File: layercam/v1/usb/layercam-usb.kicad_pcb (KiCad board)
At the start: 2 copper layers, 22 x 16 mm, 7 parts, among them J1 USB-C, J2 SH 6, U1 USBLC6-2SC6

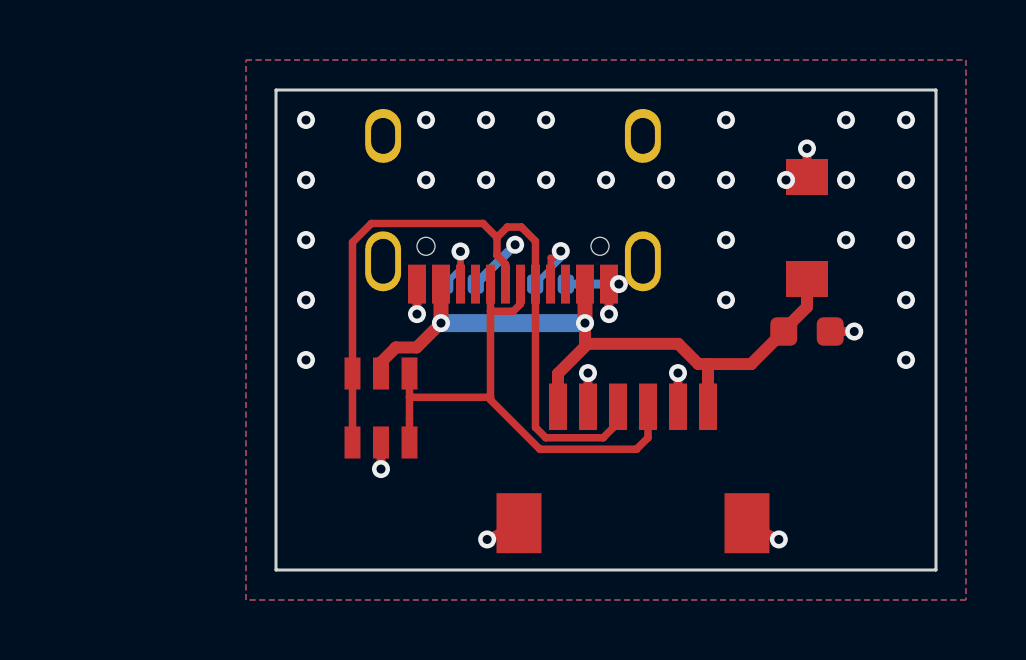
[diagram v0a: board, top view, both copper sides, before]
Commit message: layercam v1: the USB board was a mirror image of its slot; fixed
Placed as a real rotation (its parts' face towards the opening), the
board's x runs along the slot's -v, but it had been drawn with x = v: its
14.1 mm side would have met the wall where the grooves allow 7.9 mm.
Found while building the 3D assembly; a board-sized block on the case's
own mesh confirms it (783 of 4455 sample points inside the plastic one
way, none the other).

The board now runs x -14.1 .. 7.9 (geometry.USB_BOX), its parts mirrored
to match, re-routed: DRC 0 / 0 / 0, every gate.  verify.py gains the check
its docstring promised: the USB board's outline from its board file, in
the grooves.

Co-Authored-By: Claude Opus 5.5 <noreply@anthropic.com>
Claude-Session: https://claude.ai/code/session_01SRhEBojLChjJZAxgunyC3D
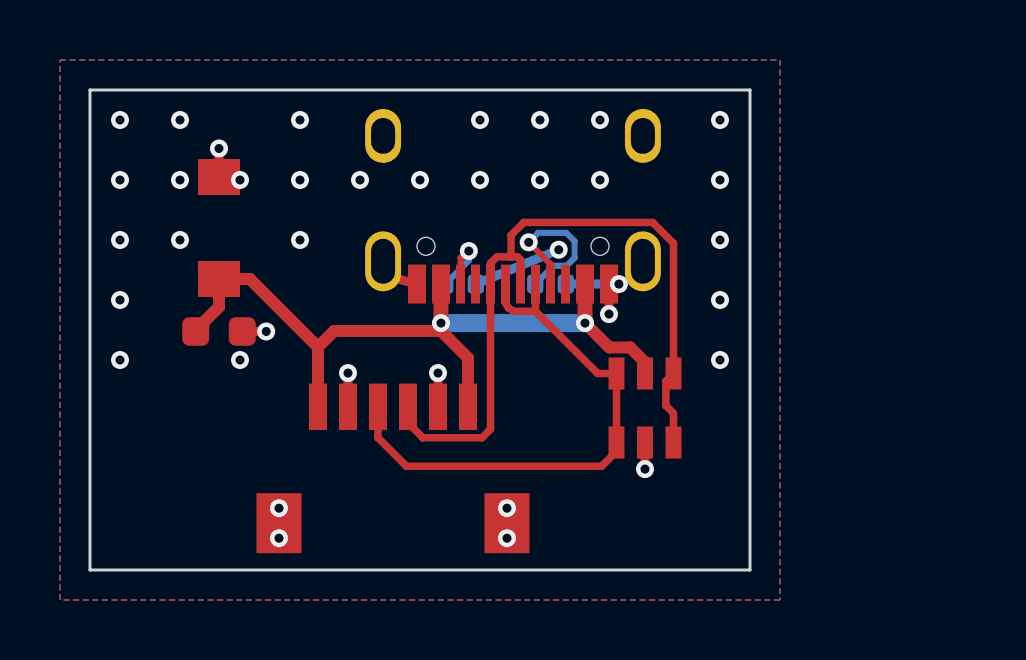
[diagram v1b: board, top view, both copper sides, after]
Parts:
- D1: value SMF5.0CA -> SMF6.0CA
- moved C1 19.6 mm to (90.2, 108.0)
- moved D1 19.6 mm to (90.2, 104.6)
- moved U1 8.80 mm to (104.4, 110.6)
- moved J2 8.00 mm to (96.0, 112.5)
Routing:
- net USB_DP: track 17.7 -> 24.5 mm
- net USB_DM: track 25.1 -> 18.4 mm
- net CC1: track 2.77 -> 5.71 mm
- net VSYS: track 24.3 -> 26.1 mm
- net GND: track 12.9 -> 11.2 mm, vias 37 -> 38

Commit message: LayerCam v1: rebuild all three boards with their badges
The OffGrid lockup, each board's name and revision, and the US flag on
the USB-C board, on the silkscreen of every board. DRC 0/0/0 on all
three. README: the console and boot pads are no longer labelled.

Co-Authored-By: Claude Opus 5.5 <noreply@anthropic.com>
Claude-Session: https://claude.ai/code/session_01SRhEBojLChjJZAxgunyC3D
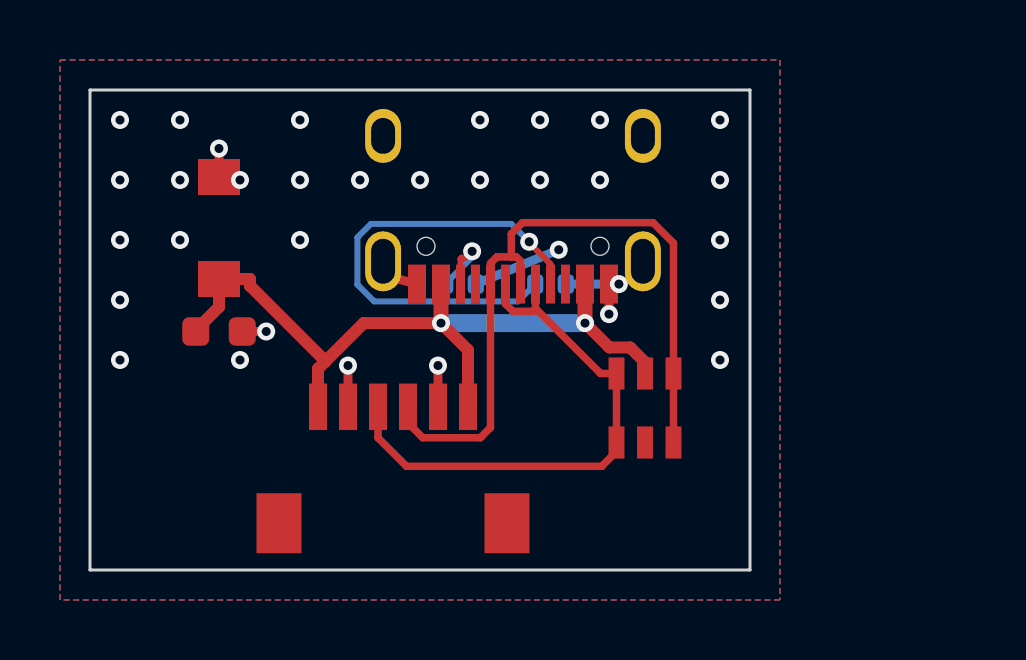
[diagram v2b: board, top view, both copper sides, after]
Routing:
- net CC1: track 5.71 -> 15.8 mm
- net GND: track 11.2 -> 10.9 mm, vias 38 -> 33
